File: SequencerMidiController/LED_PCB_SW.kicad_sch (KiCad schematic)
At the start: 1 part, among them U9 PCB-SPST_RGB-LED-Counter-Cloc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

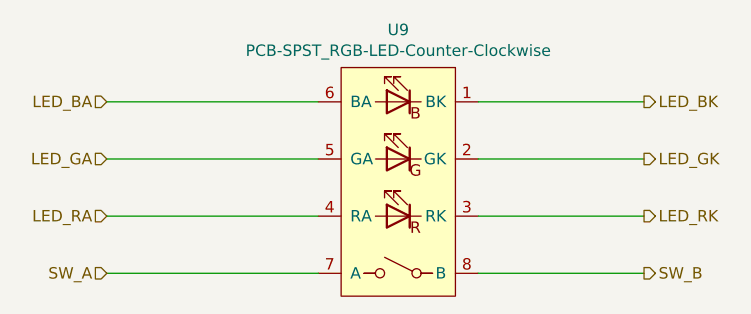
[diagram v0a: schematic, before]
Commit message: updated layout DRC
Fixed clearance errors with polygons and pads in switch footprints
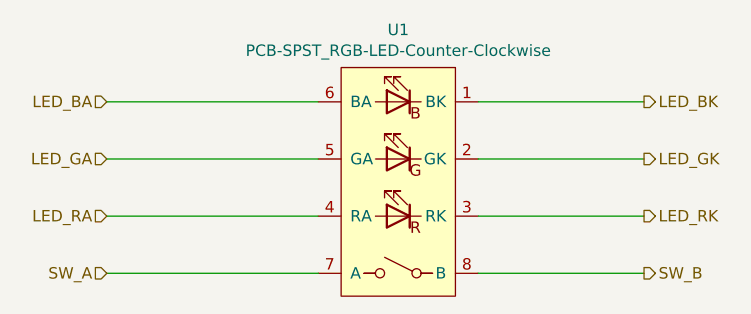
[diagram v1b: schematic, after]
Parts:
- renumbered U9 to U1
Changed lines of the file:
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@@
   (symbol (lib_id "PCB_LED_SW:PCB-SPST_RGB-LED-Counter-Clockwise") (at 158.115 97.79 0) (mirror y)
     (in_bom yes) (on_board yes)
-    (property "Reference" "U9" (id 0) (at 158.115 80.899 0))
+    (property "Reference" "U1" (id 0) (at 158.115 80.899 0))
     (property "Value" "PCB-SPST_RGB-LED-Counter-Clockwise" (id 1) (at 158.115 83.2104 0))
     (property "Footprint" "PCB_SW_LED:Circular_3mm_10mm_Cree_PLLC6_CLY6D-FKC-CK1N1D1BB7D3D3" (id 2) (at 158.115 82.55 0)
